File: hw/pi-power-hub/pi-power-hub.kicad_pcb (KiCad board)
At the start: 2 copper layers, 99.9 x 150 mm, 75 parts, among them J1 USB_A, J10 USB_A, J2 USB_A, J3 USB_A, J4 Conn_01x04_Male, J5 USB_B_Micro, J6 USB_B_Micro, J7 USB_A, J8 Conn_01x02_Male, J9 USB_A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

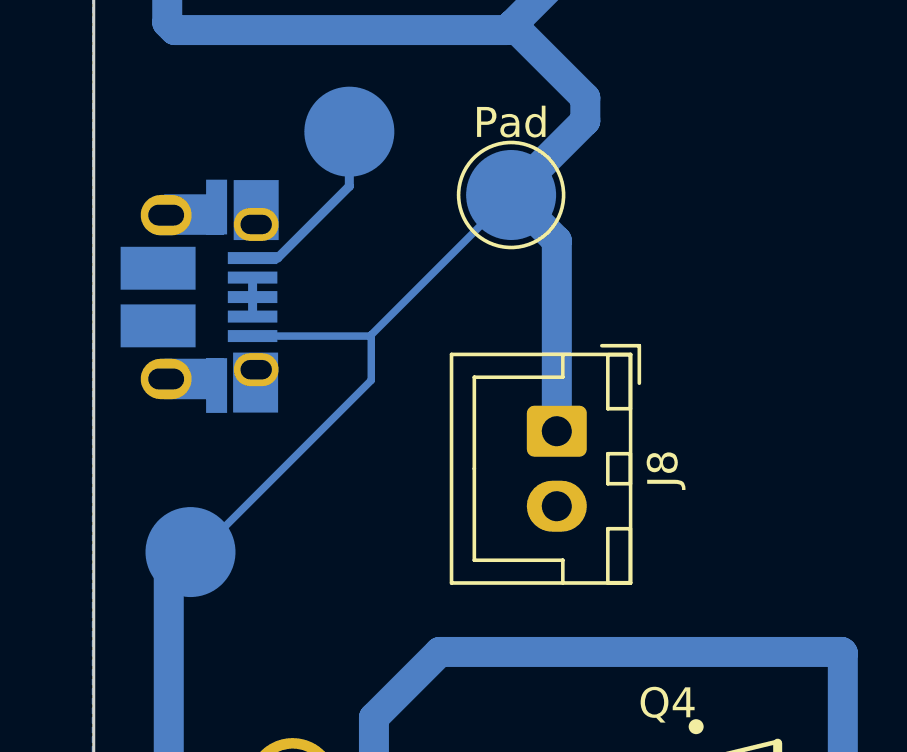
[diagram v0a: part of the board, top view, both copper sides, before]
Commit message: Change output pins order
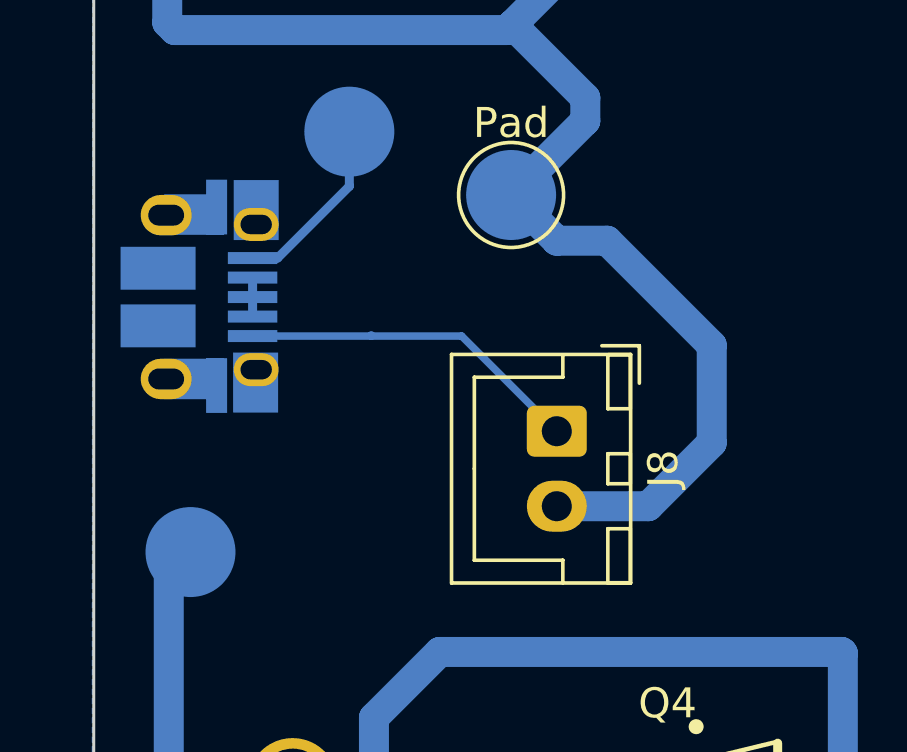
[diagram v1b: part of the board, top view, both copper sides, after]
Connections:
- J6 pad 1: Net-(J6-Pad1) -> 5V_Switched
- J8 pad 1: 5V -> 5V_Switched
- J8 pad 2: Net-(J6-Pad1) -> 5V
- SW1 pad 2: PORT_1_BTN -> PORT_3_BTN
- SW2 pad 2: PORT_3_BTN -> PORT_1_BTN
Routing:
- net 5V_Switched: track 0.00 -> 11.5 mm
- net 5V: track 397.3 -> 386.0 mm
- net PORT_3_BTN: track 20.7 -> 22.3 mm
- net PORT_1_BTN: track 20.8 -> 19.1 mm
